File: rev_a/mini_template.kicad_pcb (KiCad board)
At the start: 2 copper layers, 4 parts

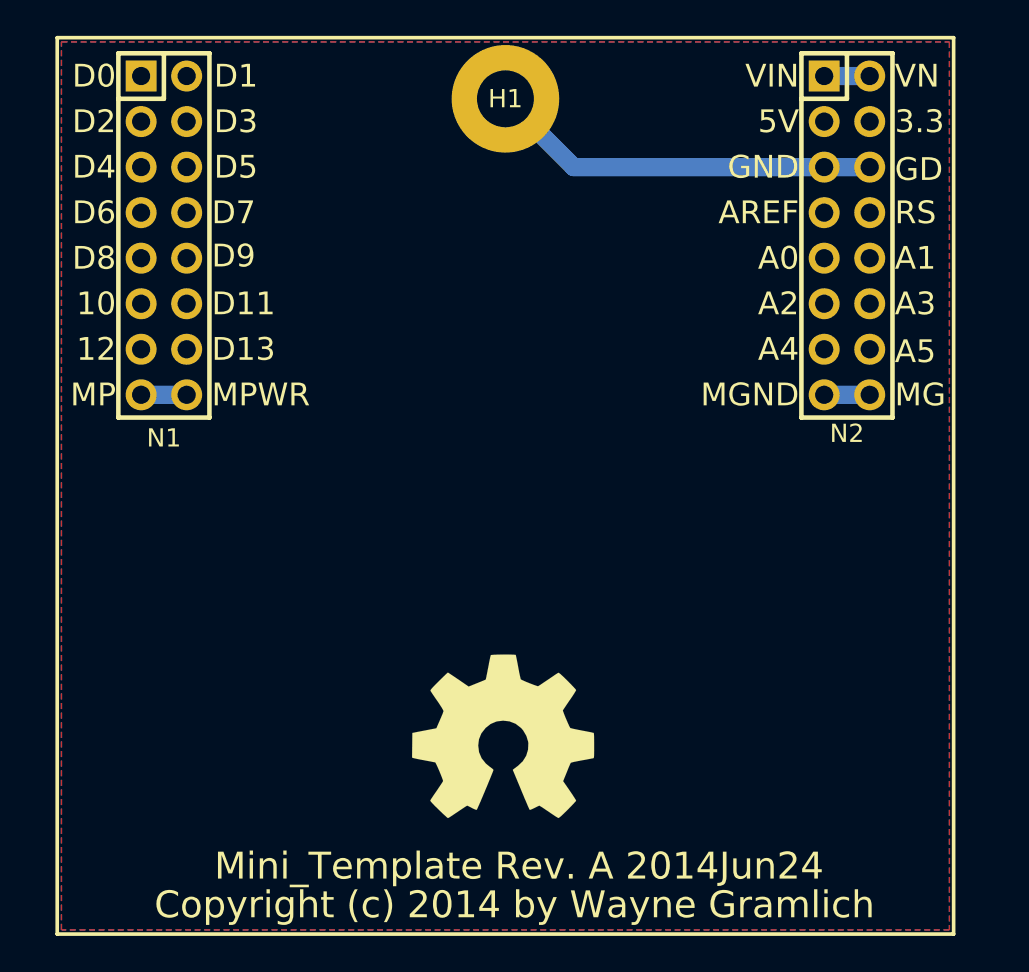
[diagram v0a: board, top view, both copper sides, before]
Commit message: Fixed open source hardware logo to have text.
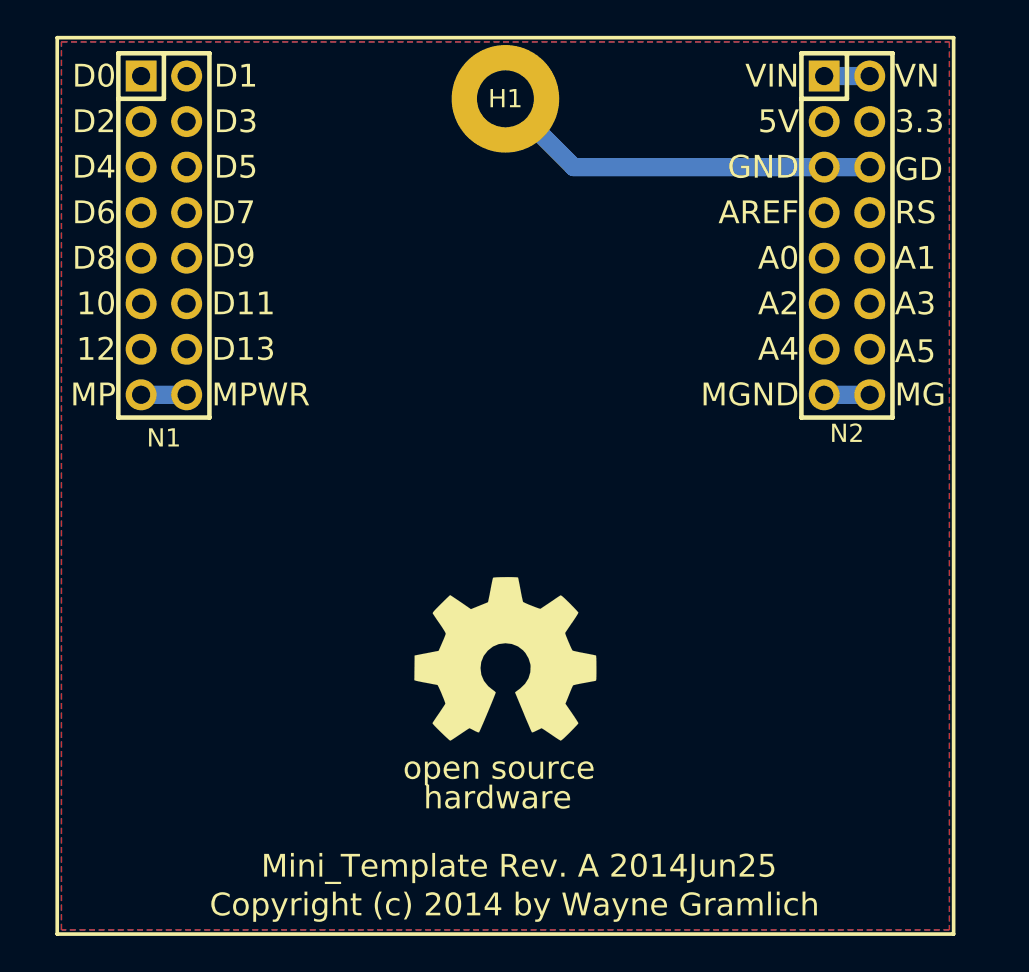
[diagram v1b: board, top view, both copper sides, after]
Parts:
- moved G1 4.32 mm to (101.6, 137.9)
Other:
- board text added: "Mini_Template Rev. A 2014Jun25"
- board text added: "hardware"
- board text added: "open source"
- board text removed: "Mini_Template Rev. A 2014Jun24"
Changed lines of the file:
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@@
     (links 5)
     (no_connects 0)
-    (area 0 0 0 0)
+    (area 71.847163 103.168398 126.701602 153.371602)
     (thickness 1.6)
-    (drawings 38)
+    (drawings 40)
     (tracks 6)
     (zones 0)
@@
   )
   (module Mini_Template_Rev_A:OSHW_LOGO_400mil (layer F.Cu)
-    (at 101.473 142.24)
-    (fp_text reference G1 (at 0 5.38734) (layer F.SilkS) hide
+    (at 101.6 137.922)
+    (fp_text reference G1 (at 2.667 1.143) (layer F.SilkS) hide
       (effects (font (size 0.46228 0.46228) (thickness 0.09144)))
     )
@@
       (xy -3.07848 4.56184)) (layer F.SilkS) (width 0.00254))
   )
-  (gr_text "Mini_Template Rev. A 2014Jun24" (at 102.362 149.479) (layer F.SilkS)
-    (effects (font (size 1.5 1.5) (thickness 0.3)))
+  (gr_text hardware (at 97.028 145.669) (layer F.SilkS)
+    (effects (font (size 1.27 1.27) (thickness 0.2032)) (justify left))
+  )
+  (gr_text "open source" (at 95.885 144.018) (layer F.SilkS)
+    (effects (font (size 1.27 1.27) (thickness 0.2032)) (justify left))
+  )
+  (gr_text "Mini_Template Rev. A 2014Jun25" (at 102.362 149.479) (layer F.SilkS)
+    (effects (font (size 1.27 1.27) (thickness 0.2032)))
   )
   (gr_text "Copyright (c) 2014 by Wayne Gramlich" (at 102.108 151.638) (layer F.SilkS)
-    (effects (font (size 1.5 1.5) (thickness 0.3)))
+    (effects (font (size 1.27 1.27) (thickness 0.2032)))
   )
   (gr_text A5 (at 123.317 120.777) (layer F.SilkS)
@@
   (gr_line (start 76.599999 103.269999) (end 76.599999 153.270001) (angle 90) (layer F.SilkS) (width 0.2032))
   (gr_line (start 76.599999 103.269999) (end 126.600001 103.269999) (angle 90) (layer F.SilkS) (width 0.2032))
+  (segment (start 105.41 110.49) (end 101.6 106.68) (width 1.016) (layer B.Cu) (net 1))
+  (segment (start 119.38 110.49) (end 105.41 110.49) (width 1.016) (layer B.Cu) (net 1))
   (segment (start 121.92 110.49) (end 119.38 110.49) (width 1.016) (layer B.Cu) (net 1))
-  (segment (start 119.38 110.49) (end 105.41 110.49) (width 1.016) (layer B.Cu) (net 1))
-  (segment (start 105.41 110.49) (end 101.6 106.68) (width 1.016) (layer B.Cu) (net 1))
   (segment (start 83.82 123.19) (end 81.28 123.19) (width 1.016) (layer B.Cu) (net 2))
   (segment (start 121.92 105.41) (end 119.38 105.41) (width 1.016) (layer B.Cu) (net 3))
